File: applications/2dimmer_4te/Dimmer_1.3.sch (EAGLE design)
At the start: 41 parts, among them IC1 CNY17, IC2 89LPC922, IC3 CNY17, IC4 CNY17, K1 ISP, Q1 IRFP460, Q2 IRFP460, Q3 IRFP460, Q4 IRFP460

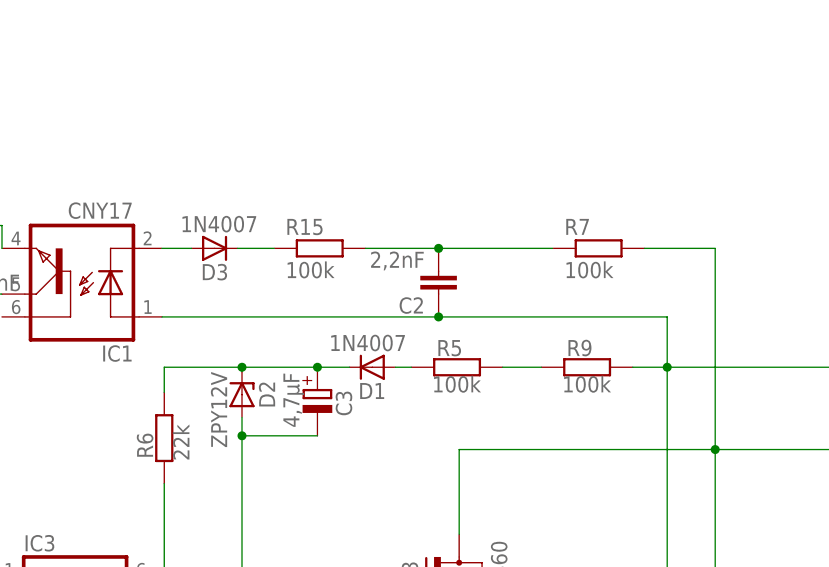
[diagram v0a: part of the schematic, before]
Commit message: 2,2nF mit X2 gekennzeichnet
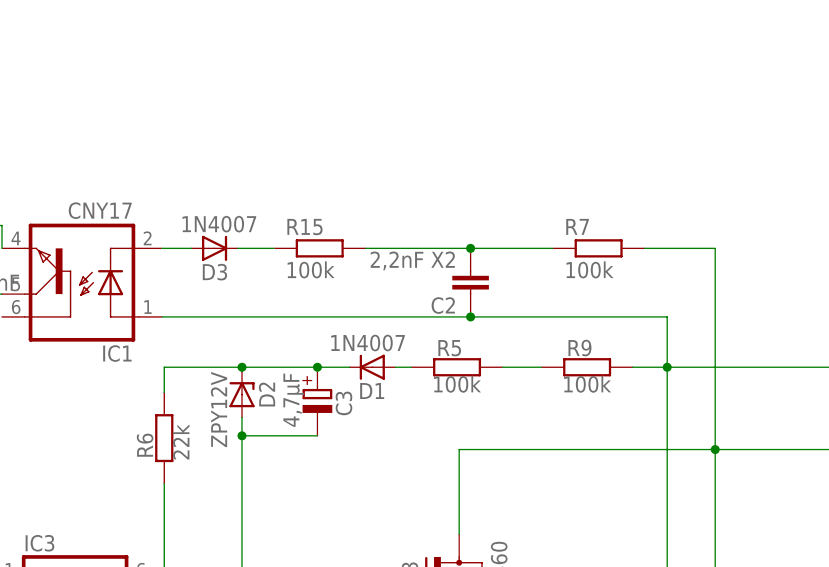
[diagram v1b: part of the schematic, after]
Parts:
- C2: value 2,2nF -> 2,2nF X2
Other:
- moved on the sheet: C2
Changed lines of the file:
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@@
 <part name="R8" library="rcl" deviceset="R-EU_" device="0204/7" value="100k"/>
 <part name="R9" library="rcl" deviceset="R-EU_" device="0204/7" value="100k"/>
-<part name="C2" library="rcl" deviceset="C-EU" device="075-063X106" value="2,2nF"/>
+<part name="C2" library="rcl" deviceset="C-EU" device="075-063X106" value="2,2nF X2"/>
 <part name="D3" library="diode" deviceset="1N4148" device="" value="1N4007"/>
 <part name="R15" library="rcl" deviceset="R-EU_" device="0204/7" value="100k"/>
@@
 <attribute name="VALUE" x="170.172" y="126.238" size="1.778" layer="96"/>
 </instance>
-<instance part="C2" gate="G$1" x="156.464" y="137.16" rot="R180"/>
+<instance part="C2" gate="G$1" x="160.02" y="137.16" rot="R180"/>
 <instance part="D3" gate="G$1" x="131.572" y="142.24" smashed="yes" rot="MR180">
 <attribute name="NAME" x="130.048" y="140.4874" size="1.778" layer="95" rot="MR180"/>
@@
 <net name="N$3" class="0">
 <segment>
-<wire x1="125.73" y1="134.62" x2="156.464" y2="134.62" width="0.1524" layer="91"/>
-<wire x1="156.464" y1="134.62" x2="181.864" y2="134.62" width="0.1524" layer="91"/>
+<wire x1="125.73" y1="134.62" x2="160.02" y2="134.62" width="0.1524" layer="91"/>
+<wire x1="160.02" y1="134.62" x2="181.864" y2="134.62" width="0.1524" layer="91"/>
 <wire x1="181.864" y1="134.62" x2="181.864" y2="129.032" width="0.1524" layer="91"/>
 <wire x1="181.864" y1="129.032" x2="207.01" y2="129.032" width="0.1524" layer="91"/>
@@
 <wire x1="178.046" y1="129.032" x2="181.864" y2="129.032" width="0.1524" layer="91"/>
 <pinref part="C2" gate="G$1" pin="1"/>
-<junction x="156.464" y="134.62"/>
+<junction x="160.02" y="134.62"/>
 </segment>
 </net>
@@
 <pinref part="R7" gate="G$1" pin="1"/>
 <pinref part="C2" gate="G$1" pin="2"/>
-<wire x1="148.336" y1="142.24" x2="156.464" y2="142.24" width="0.1524" layer="91"/>
-<wire x1="156.464" y1="142.24" x2="169.164" y2="142.24" width="0.1524" layer="91"/>
-<junction x="156.464" y="142.24"/>
+<wire x1="148.336" y1="142.24" x2="160.02" y2="142.24" width="0.1524" layer="91"/>
+<wire x1="160.02" y1="142.24" x2="169.164" y2="142.24" width="0.1524" layer="91"/>
+<junction x="160.02" y="142.24"/>
 <pinref part="R15" gate="G$1" pin="2"/>
 </segment>
